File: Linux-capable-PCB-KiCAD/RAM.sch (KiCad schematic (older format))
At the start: 24 parts

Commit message: added ESD protection, g sensor
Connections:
- net labels added: adr0, adr1, adr10, adr11, adr12, adr13, adr14, adr2, adr3, adr4, adr5, adr6, adr7, adr8, adr9
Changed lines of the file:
@@
 $Descr A4 11693 8268
 encoding utf-8
-Sheet 4 4
+Sheet 4 5
 Title ""
 Date ""
@@
 Wire Wire Line
 	1500 2225 1825 2225
+Entry Bus Bus
+	1400 3725 1500 3625
+Text Label 1600 2225 0    0    ~ 0
+adr0
+Text Label 1575 2225 0    50   ~ 0
+adr0
+Text Label 1575 2325 0    50   ~ 0
+adr1
+Text Label 1575 2425 0    50   ~ 0
+adr2
+Text Label 1575 2525 0    50   ~ 0
+adr3
+Text Label 1575 2625 0    50   ~ 0
+adr4
+Text Label 1575 2725 0    50   ~ 0
+adr5
 Wire Bus Line
 	1425 3975 1425 4175
@@
 Wire Bus Line
 	1400 2325 1400 3725
-Entry Bus Bus
-	1400 3725 1500 3625
+Text Label 1575 2825 0    50   ~ 0
+adr6
+Text Label 1575 2925 0    50   ~ 0
+adr7
+Text Label 1575 3025 0    50   ~ 0
+adr8
+Text Label 1575 3125 0    50   ~ 0
+adr9
+Text Label 1575 3225 0    50   ~ 0
+adr10
+Text Label 1575 3325 0    50   ~ 0
+adr11
+Text Label 1575 3425 0    50   ~ 0
+adr12
+Text Label 1575 3525 0    50   ~ 0
+adr13
+Text Label 1575 3625 0    50   ~ 0
+adr14
 $EndSCHEMATC

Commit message: Power supply schematics
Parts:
- C46, C47, C48, C49, C50, C51, C52, C53, C54, C55, C56, C57, C58, C59, C60, C61, C62, C63, C64: renamed from C?; symbol Device:C -> Linux-capable-PCB-KiCAD-rescue:C-Device
- R19, R20, R21: renamed from R?; symbol Device:R -> Linux-capable-PCB-KiCAD-rescue:R-Device
- gave numbers to parts that had none: 1

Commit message: Assigned footprints to components, antenna and a couple of other footprints need to be assigned
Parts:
- C46, C47, C48, C49, C50, C51, C52, C53, C54, C55, C56, C57, C58, C59, C60, C61, C62, C63, C64: footprint (none) -> Capacitor_SMD:C_0603_1608Metric
- R19, R20, R21: footprint (none) -> Resistor_SMD:R_0603_1608Metric
- U8: footprint (none) -> Package_BGA:BGA-96_9.0x13.0mm_Layout2x3x16_P0.8mm
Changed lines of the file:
@@
 F 0 "U8" H 9625 4765 50  0000 C CNN
 F 1 "HTQ4G63AFR-PCB" H 9625 4674 50  0000 C CNN
-F 2 "" H 9425 3900 50  0001 C CNN
+F 2 "Package_BGA:BGA-96_9.0x13.0mm_Layout2x3x16_P0.8mm" H 9425 3900 50  0001 C CNN
 F 3 "" H 9425 3900 50  0001 C CNN
 	1    9625 3300
@@
 F 0 "U8" H 2325 4090 50  0000 C CNN
 F 1 "HTQ4G63AFR-PCB" H 2325 3999 50  0000 C CNN
-F 2 "" H 2075 3625 50  0001 C CNN
+F 2 "Package_BGA:BGA-96_9.0x13.0mm_Layout2x3x16_P0.8mm" H 2075 3625 50  0001 C CNN
 F 3 "" H 2075 3625 50  0001 C CNN
 	2    2275 3025
@@
 F 0 "C64" H 9015 4996 50  0000 L CNN
 F 1 "100n" H 8925 4850 50  0000 L CNN
-F 2 "" H 8938 4800 50  0001 C CNN
+F 2 "Capacitor_SMD:C_0603_1608Metric" H 8938 4800 50  0001 C CNN
 F 3 "~" H 8900 4950 50  0001 C CNN
 	1    8900 4950
@@
 F 0 "C63" H 8615 4996 50  0000 L CNN
 F 1 "100n" H 8525 4850 50  0000 L CNN
-F 2 "" H 8538 4800 50  0001 C CNN
+F 2 "Capacitor_SMD:C_0603_1608Metric" H 8538 4800 50  0001 C CNN
 F 3 "~" H 8500 4950 50  0001 C CNN
 	1    8500 4950
@@
 F 0 "C61" H 8240 4996 50  0000 L CNN
 F 1 "100n" H 8150 4850 50  0000 L CNN
-F 2 "" H 8163 4800 50  0001 C CNN
+F 2 "Capacitor_SMD:C_0603_1608Metric" H 8163 4800 50  0001 C CNN
 F 3 "~" H 8125 4950 50  0001 C CNN
 	1    8125 4950
@@
 F 0 "C60" H 8240 4471 50  0000 L CNN
 F 1 "100n" H 8240 4380 50  0000 L CNN
-F 2 "" H 8163 4275 50  0001 C CNN
+F 2 "Capacitor_SMD:C_0603_1608Metric" H 8163 4275 50  0001 C CNN
 F 3 "~" H 8125 4425 50  0001 C CNN
 	1    8125 4425
@@
 F 0 "R20" H 7745 4471 50  0000 L CNN
 F 1 "1k 1%" H 7745 4380 50  0000 L CNN
-F 2 "" V 7605 4425 50  0001 C CNN
+F 2 "Resistor_SMD:R_0603_1608Metric" V 7605 4425 50  0001 C CNN
 F 3 "~" H 7675 4425 50  0001 C CNN
 	1    7675 4425
@@
 F 0 "R21" H 7745 5021 50  0000 L CNN
 F 1 "1k 1%" H 7745 4930 50  0000 L CNN
-F 2 "" V 7605 4975 50  0001 C CNN
+F 2 "Resistor_SMD:R_0603_1608Metric" V 7605 4975 50  0001 C CNN
 F 3 "~" H 7675 4975 50  0001 C CNN
 	1    7675 4975
@@
 F 0 "C49" H 4990 2021 50  0000 L CNN
 F 1 "100n" H 4900 1875 50  0000 L CNN
-F 2 "" H 4913 1825 50  0001 C CNN
+F 2 "Capacitor_SMD:C_0603_1608Metric" H 4913 1825 50  0001 C CNN
 F 3 "~" H 4875 1975 50  0001 C CNN
 	1    4875 1975
@@
 F 0 "C51" H 5365 2021 50  0000 L CNN
 F 1 "100n" H 5275 1875 50  0000 L CNN
-F 2 "" H 5288 1825 50  0001 C CNN
+F 2 "Capacitor_SMD:C_0603_1608Metric" H 5288 1825 50  0001 C CNN
 F 3 "~" H 5250 1975 50  0001 C CNN
 	1    5250 1975
@@
 F 0 "C52" H 5715 2021 50  0000 L CNN
 F 1 "100n" H 5625 1875 50  0000 L CNN
-F 2 "" H 5638 1825 50  0001 C CNN
+F 2 "Capacitor_SMD:C_0603_1608Metric" H 5638 1825 50  0001 C CNN
 F 3 "~" H 5600 1975 50  0001 C CNN
 	1    5600 1975
@@
 F 0 "C54" H 6065 2021 50  0000 L CNN
 F 1 "100n" H 5975 1875 50  0000 L CNN
-F 2 "" H 5988 1825 50  0001 C CNN
+F 2 "Capacitor_SMD:C_0603_1608Metric" H 5988 1825 50  0001 C CNN
 F 3 "~" H 5950 1975 50  0001 C CNN
 	1    5950 1975
@@
 F 0 "C55" H 6440 2021 50  0000 L CNN
 F 1 "100n" H 6350 1875 50  0000 L CNN
-F 2 "" H 6363 1825 50  0001 C CNN
+F 2 "Capacitor_SMD:C_0603_1608Metric" H 6363 1825 50  0001 C CNN
 F 3 "~" H 6325 1975 50  0001 C CNN
 	1    6325 1975
@@
 F 0 "C56" H 6815 2021 50  0000 L CNN
 F 1 "100n" H 6725 1875 50  0000 L CNN
-F 2 "" H 6738 1825 50  0001 C CNN
+F 2 "Capacitor_SMD:C_0603_1608Metric" H 6738 1825 50  0001 C CNN
 F 3 "~" H 6700 1975 50  0001 C CNN
 	1    6700 1975
@@
 F 0 "C57" H 7165 2021 50  0000 L CNN
 F 1 "100n" H 7075 1875 50  0000 L CNN
-F 2 "" H 7088 1825 50  0001 C CNN
+F 2 "Capacitor_SMD:C_0603_1608Metric" H 7088 1825 50  0001 C CNN
 F 3 "~" H 7050 1975 50  0001 C CNN
 	1    7050 1975
@@
 F 0 "C48" H 4640 2021 50  0000 L CNN
 F 1 "100n" H 4550 1875 50  0000 L CNN
-F 2 "" H 4563 1825 50  0001 C CNN
+F 2 "Capacitor_SMD:C_0603_1608Metric" H 4563 1825 50  0001 C CNN
 F 3 "~" H 4525 1975 50  0001 C CNN
 	1    4525 1975
@@
 F 0 "C58" H 7515 2021 50  0000 L CNN
 F 1 "100n" H 7425 1875 50  0000 L CNN
-F 2 "" H 7438 1825 50  0001 C CNN
+F 2 "Capacitor_SMD:C_0603_1608Metric" H 7438 1825 50  0001 C CNN
 F 3 "~" H 7400 1975 50  0001 C CNN
 	1    7400 1975
@@
 F 0 "C59" H 7940 2021 50  0000 L CNN
 F 1 "100n" H 7850 1875 50  0000 L CNN
-F 2 "" H 7863 1825 50  0001 C CNN
+F 2 "Capacitor_SMD:C_0603_1608Metric" H 7863 1825 50  0001 C CNN
 F 3 "~" H 7825 1975 50  0001 C CNN
 	1    7825 1975
@@
 F 0 "C62" H 8340 2021 50  0000 L CNN
 F 1 "100n" H 8250 1875 50  0000 L CNN
-F 2 "" H 8263 1825 50  0001 C CNN
+F 2 "Capacitor_SMD:C_0603_1608Metric" H 8263 1825 50  0001 C CNN
 F 3 "~" H 8225 1975 50  0001 C CNN
 	1    8225 1975
@@
 F 0 "C47" H 4265 2021 50  0000 L CNN
 F 1 "100n" H 4175 1875 50  0000 L CNN
-F 2 "" H 4188 1825 50  0001 C CNN
+F 2 "Capacitor_SMD:C_0603_1608Metric" H 4188 1825 50  0001 C CNN
 F 3 "~" H 4150 1975 50  0001 C CNN
 	1    4150 1975
@@
 F 0 "C46" H 3865 2021 50  0000 L CNN
 F 1 "100n" H 3775 1875 50  0000 L CNN
-F 2 "" H 3788 1825 50  0001 C CNN
+F 2 "Capacitor_SMD:C_0603_1608Metric" H 3788 1825 50  0001 C CNN
 F 3 "~" H 3750 1975 50  0001 C CNN
 	1    3750 1975
@@
 F 0 "C53" H 5840 3446 50  0000 L CNN
 F 1 "100n" H 5840 3355 50  0000 L CNN
-F 2 "" H 5763 3250 50  0001 C CNN
+F 2 "Capacitor_SMD:C_0603_1608Metric" H 5763 3250 50  0001 C CNN
 F 3 "~" H 5725 3400 50  0001 C CNN
 	1    5725 3400
@@
 F 0 "C50" H 5340 3446 50  0000 L CNN
 F 1 "100n" H 5340 3355 50  0000 L CNN
-F 2 "" H 5263 3250 50  0001 C CNN
+F 2 "Capacitor_SMD:C_0603_1608Metric" H 5263 3250 50  0001 C CNN
 F 3 "~" H 5225 3400 50  0001 C CNN
 	1    5225 3400
@@
 F 0 "R19" V 3300 5050 50  0000 C CNN
 F 1 "240R" V 3200 5125 50  0000 C CNN
-F 2 "" V 3130 5125 50  0001 C CNN
+F 2 "Resistor_SMD:R_0603_1608Metric" V 3130 5125 50  0001 C CNN
 F 3 "~" H 3200 5125 50  0001 C CNN
 	1    3200 5125

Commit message: CPU and RAM
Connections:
- net labels added: CK_N, CK_P
- net labels removed: CK, ~CK
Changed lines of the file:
@@
 ~CKE
 Text HLabel 1475 4675 0    50   Input ~ 0
-CK
+CK_P
 Text HLabel 1475 4575 0    50   Input ~ 0
-~CK
+CK_N
 Text HLabel 1475 4375 0    50   Input ~ 0
 ~RAS

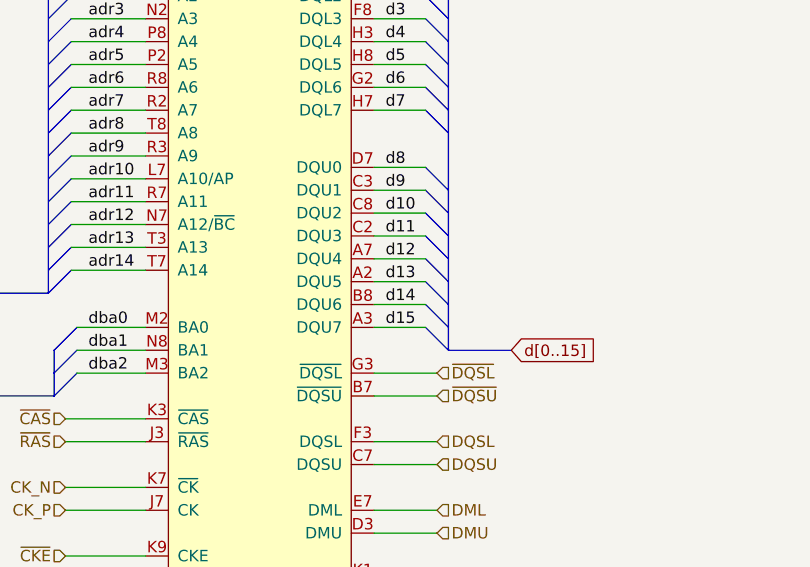
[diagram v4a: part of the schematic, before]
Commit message: DDR3 - CPU layout
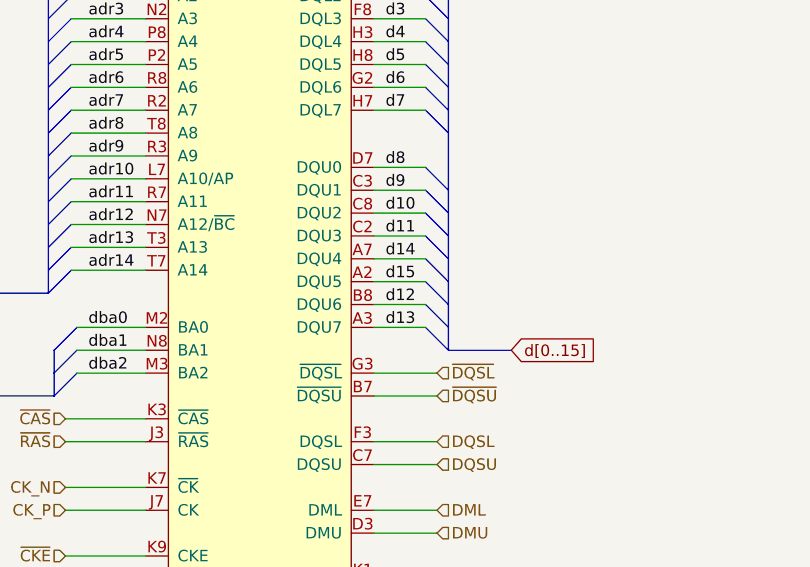
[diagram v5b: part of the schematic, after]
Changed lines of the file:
@@
 Text Label 2875 3475 0    50   ~ 0
 d11
+Text Label 2875 3775 0    50   ~ 0
+d12
+Text Label 2875 3875 0    50   ~ 0
+d13
 Text Label 2875 3575 0    50   ~ 0
-d12
+d14
 Text Label 2875 3675 0    50   ~ 0
-d13
-Text Label 2875 3775 0    50   ~ 0
-d14
-Text Label 2875 3875 0    50   ~ 0
 d15
 Entry Bus Bus

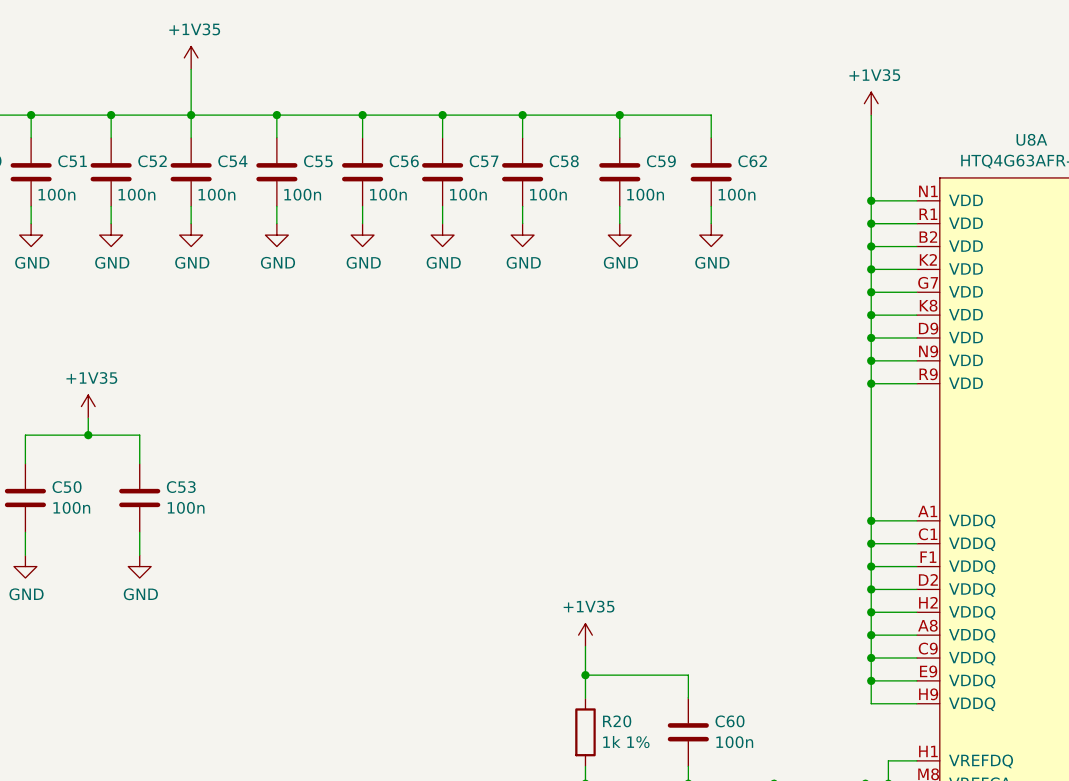
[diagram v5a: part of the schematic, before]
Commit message: CPU and DDR3 connected
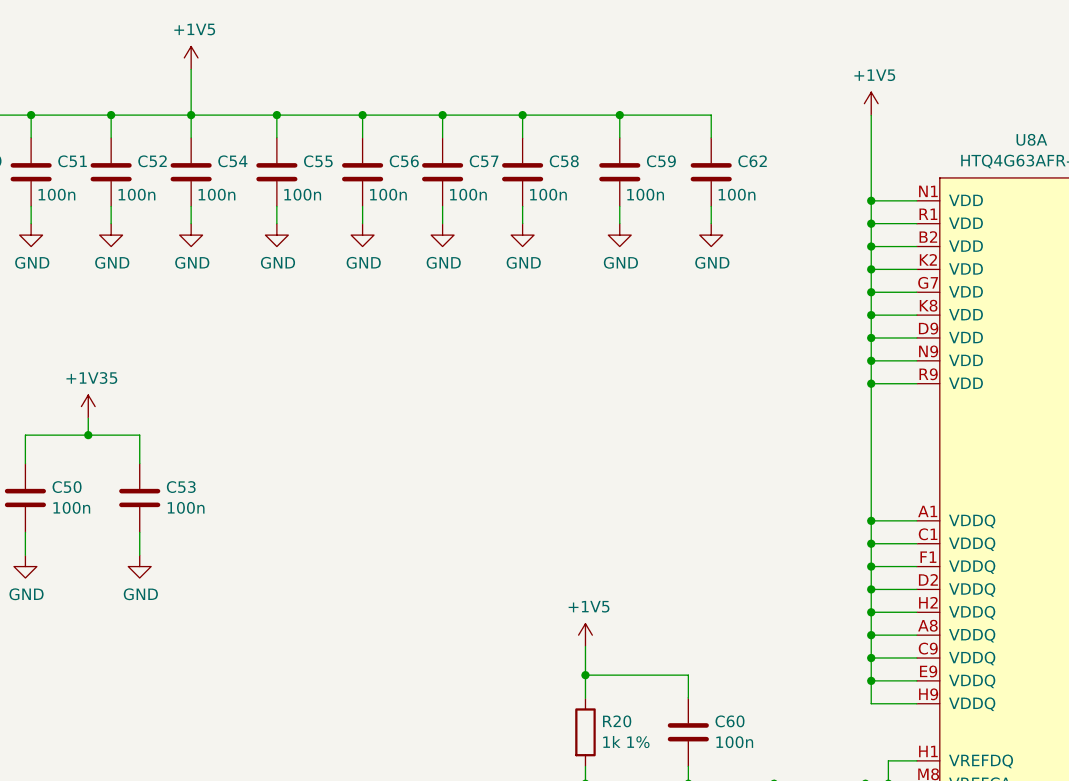
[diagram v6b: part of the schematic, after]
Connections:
- net labels added: +1V5
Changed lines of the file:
@@
 Comment4 ""
 $EndDescr
-$Comp
-L H5TQ4G63AFR-PCB:HTQ4G63AFR-PCB U8
-U 1 1 62BBB4D5
-P 9625 3300
-F 0 "U8" H 9625 4765 50  0000 C CNN
-F 1 "HTQ4G63AFR-PCB" H 9625 4674 50  0000 C CNN
-F 2 "Package_BGA:BGA-96_9.0x13.0mm_Layout2x3x16_P0.8mm" H 9425 3900 50  0001 C CNN
-F 3 "" H 9425 3900 50  0001 C CNN
-	1    9625 3300
-	1    0    0    -1
-$EndComp
-$Comp
-L H5TQ4G63AFR-PCB:HTQ4G63AFR-PCB U8
-U 2 1 62BBDB89
-P 2275 3025
-F 0 "U8" H 2325 4090 50  0000 C CNN
-F 1 "HTQ4G63AFR-PCB" H 2325 3999 50  0000 C CNN
-F 2 "Package_BGA:BGA-96_9.0x13.0mm_Layout2x3x16_P0.8mm" H 2075 3625 50  0001 C CNN
-F 3 "" H 2075 3625 50  0001 C CNN
-	2    2275 3025
-	1    0    0    -1
-$EndComp
 Wire Wire Line
 	10125 2100 10350 2100
@@
 Wire Wire Line
 	8925 2200 8925 2300
-$Comp
-L power:+1V35 #PWR0190
-U 1 1 62BDED23
-P 8925 1725
-F 0 "#PWR0190" H 8925 1575 50  0001 C CNN
-F 1 "+1V35" H 8940 1898 50  0000 C CNN
-F 2 "" H 8925 1725 50  0001 C CNN
-F 3 "" H 8925 1725 50  0001 C CNN
-	1    8925 1725
-	1    0    0    -1
-$EndComp
 Wire Wire Line
 	8925 1725 8925 2100
@@
 Wire Wire Line
 	7675 4175 7675 4275
-$Comp
-L power:+1V35 #PWR0191
-U 1 1 62BF9E2F
-P 7675 4050
-F 0 "#PWR0191" H 7675 3900 50  0001 C CNN
-F 1 "+1V35" H 7690 4223 50  0000 C CNN
-F 2 "" H 7675 4050 50  0001 C CNN
-F 3 "" H 7675 4050 50  0001 C CNN
-	1    7675 4050
-	1    0    0    -1
-$EndComp
 Wire Wire Line
 	7675 4050 7675 4175
@@
 Wire Wire Line
 	4150 1725 4525 1725
-$Comp
-L power:+1V35 #PWR0196
-U 1 1 62C5CAB2
-P 5950 1525
-F 0 "#PWR0196" H 5950 1375 50  0001 C CNN
-F 1 "+1V35" H 5965 1698 50  0000 C CNN
-F 2 "" H 5950 1525 50  0001 C CNN
-F 3 "" H 5950 1525 50  0001 C CNN
-	1    5950 1525
-	1    0    0    -1
-$EndComp
 Wire Wire Line
 	5950 1525 5950 1725
@@
 Wire Wire Line
 	2825 4975 3100 4975
-Entry Bus Bus
-	3150 2325 3050 2225
-Entry Bus Bus
-	3150 2425 3050 2325
-Entry Bus Bus
-	3150 2525 3050 2425
-Entry Bus Bus
-	3150 2625 3050 2525
-Entry Bus Bus
-	3150 2725 3050 2625
-Entry Bus Bus
-	3150 2825 3050 2725
-Entry Bus Bus
-	3150 2925 3050 2825
-Entry Bus Bus
-	3150 3025 3050 2925
-Entry Bus Bus
-	3150 3275 3050 3175
-Entry Bus Bus
-	3150 3375 3050 3275
-Entry Bus Bus
-	3150 3475 3050 3375
-Entry Bus Bus
-	3150 3575 3050 3475
-Entry Bus Bus
-	3150 3675 3050 3575
-Entry Bus Bus
-	3150 3775 3050 3675
-Entry Bus Bus
-	3150 3875 3050 3775
-Entry Bus Bus
-	3150 3975 3050 3875
-Wire Bus Line
-	3150 3975 3425 3975
-Text GLabel 3425 3975 2    50   Input ~ 0
-d[0..15]
 Wire Wire Line
 	2825 2225 3050 2225
@@
 Text Label 1575 3625 0    50   ~ 0
 adr14
+$Comp
+L power:+1V5 #PWR0190
+U 1 1 62C609DF
+P 8925 1725
+F 0 "#PWR0190" H 8925 1575 50  0001 C CNN
+F 1 "+1V5" H 8940 1898 50  0000 C CNN
+F 2 "" H 8925 1725 50  0001 C CNN
+F 3 "" H 8925 1725 50  0001 C CNN
+	1    8925 1725
+	1    0    0    -1
+$EndComp
+$Comp
+L power:+1V5 #PWR0191
+U 1 1 62C60DED
+P 5950 1525
+F 0 "#PWR0191" H 5950 1375 50  0001 C CNN
+F 1 "+1V5" H 5965 1698 50  0000 C CNN
+F 2 "" H 5950 1525 50  0001 C CNN
+F 3 "" H 5950 1525 50  0001 C CNN
+	1    5950 1525
+	1    0    0    -1
+$EndComp
+$Comp
+L power:+1V5 #PWR0196
+U 1 1 62C617DB
+P 7675 4050
+F 0 "#PWR0196" H 7675 3900 50  0001 C CNN
+F 1 "+1V5" H 7690 4223 50  0000 C CNN
+F 2 "" H 7675 4050 50  0001 C CNN
+F 3 "" H 7675 4050 50  0001 C CNN
+	1    7675 4050
+	1    0    0    -1
+$EndComp
+$Comp
+L H5TQ4G63AFR-PCB:HTQ4G63AFR-PCB U8
+U 1 1 62C71532
+P 9625 3300
+F 0 "U8" H 9625 4765 50  0000 C CNN
+F 1 "HTQ4G63AFR-PCB" H 9625 4674 50  0000 C CNN
+F 2 "Package_BGA:BGA-96_9.0x13.0mm_Layout2x3x16_P0.8mm" H 9425 3900 50  0001 C CNN
+F 3 "" H 9425 3900 50  0001 C CNN
+	1    9625 3300
+	1    0    0    -1
+$EndComp
+$Comp
+L H5TQ4G63AFR-PCB:HTQ4G63AFR-PCB U8
+U 2 1 62C76865
+P 2275 3025
+F 0 "U8" H 2325 4090 50  0000 C CNN
+F 1 "HTQ4G63AFR-PCB" H 2325 3999 50  0000 C CNN
+F 2 "Package_BGA:BGA-96_9.0x13.0mm_Layout2x3x16_P0.8mm" H 2075 3625 50  0001 C CNN
+F 3 "" H 2075 3625 50  0001 C CNN
+	2    2275 3025
+	1    0    0    -1
+$EndComp
+Wire Bus Line
+	1400 2325 1400 3725
 Wire Bus Line
 	1425 3975 1425 4175
 Wire Bus Line
 	3150 2325 3150 3975
+Text GLabel 3425 3975 2    50   Input ~ 0
+d[0..15]
 Wire Bus Line
-	1400 2325 1400 3725
+	3150 3975 3425 3975
+Entry Bus Bus
+	3150 3975 3050 3875
+Entry Bus Bus
+	3150 3875 3050 3775
+Entry Bus Bus
+	3150 3775 3050 3675
+Entry Bus Bus
+	3150 3675 3050 3575
+Entry Bus Bus
+	3150 3575 3050 3475
+Entry Bus Bus
+	3150 3475 3050 3375
+Entry Bus Bus
+	3150 3375 3050 3275
+Entry Bus Bus
+	3150 3275 3050 3175
+Entry Bus Bus
+	3150 3025 3050 2925
+Entry Bus Bus
+	3150 2925 3050 2825
+Entry Bus Bus
+	3150 2825 3050 2725
+Entry Bus Bus
+	3150 2725 3050 2625
+Entry Bus Bus
+	3150 2625 3050 2525
+Entry Bus Bus
+	3150 2525 3050 2425
+Entry Bus Bus
+	3150 2425 3050 2325
+Entry Bus Bus
+	3150 2325 3050 2225
 $EndSCHEMATC
